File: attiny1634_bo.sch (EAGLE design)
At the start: 11 parts, among them J1 AVR_SPI_PRG_6NS, Y1 12MHz

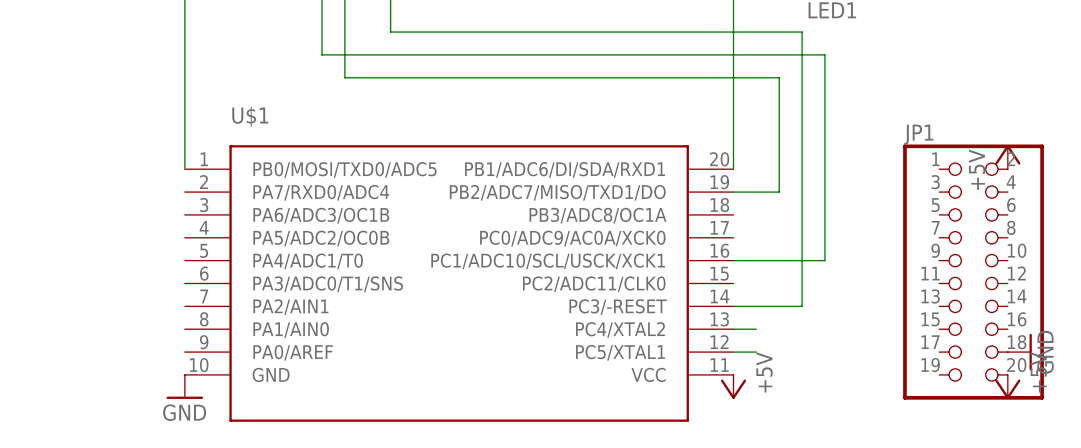
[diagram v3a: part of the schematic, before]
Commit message: connected portA
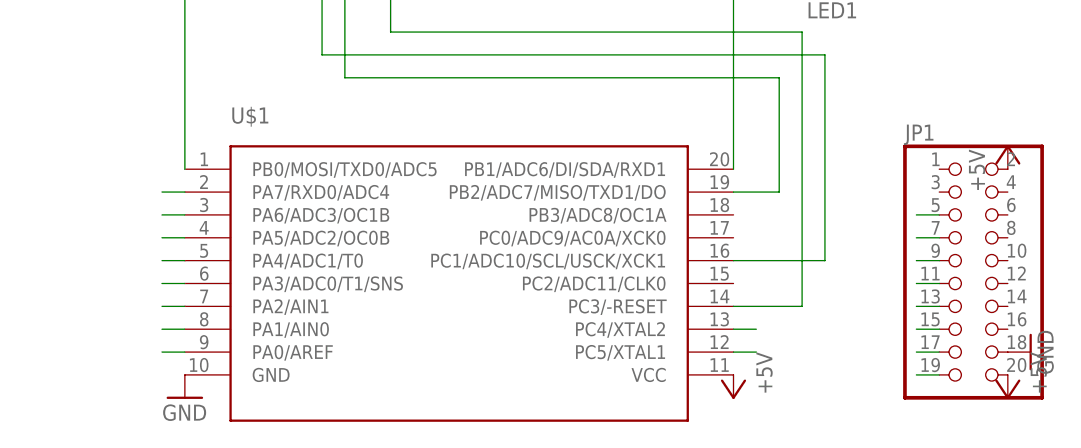
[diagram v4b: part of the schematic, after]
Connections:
- new net PA0: JP1.5, U$1.PA0/AREF
- new net PA1: JP1.7, U$1.PA1/AIN0
- new net PA2: JP1.9, U$1.PA2/AIN1
- new net PA3: JP1.11, U$1.PA3/ADC0/T1/SNS
- new net PA4: JP1.13, U$1.PA4/ADC1/T0
- new net PA5: JP1.15, U$1.PA5/ADC2/OC0B
- new net PA6: JP1.17, U$1.PA6/ADC3/OC1B
- new net PA7: JP1.19, U$1.PA7/RXD0/ADC4
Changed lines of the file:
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@@
+</segment>
+</net>
+<net name="PA0" class="0">
+<segment>
+<pinref part="U$1" gate="G$1" pin="PA0/AREF"/>
+<wire x1="35.56" y1="50.8" x2="33.02" y2="50.8" width="0.1524" layer="91"/>
+</segment>
+<segment>
+<pinref part="JP1" gate="A" pin="5"/>
+<wire x1="119.38" y1="66.04" x2="116.84" y2="66.04" width="0.1524" layer="91"/>
+</segment>
+</net>
+<net name="PA1" class="0">
+<segment>
+<pinref part="U$1" gate="G$1" pin="PA1/AIN0"/>
+<wire x1="35.56" y1="53.34" x2="33.02" y2="53.34" width="0.1524" layer="91"/>
+</segment>
+<segment>
+<pinref part="JP1" gate="A" pin="7"/>
+<wire x1="119.38" y1="63.5" x2="116.84" y2="63.5" width="0.1524" layer="91"/>
+</segment>
+</net>
+<net name="PA5" class="0">
+<segment>
+<pinref part="JP1" gate="A" pin="15"/>
+<wire x1="119.38" y1="53.34" x2="116.84" y2="53.34" width="0.1524" layer="91"/>
+</segment>
+<segment>
+<pinref part="U$1" gate="G$1" pin="PA5/ADC2/OC0B"/>
+<wire x1="35.56" y1="63.5" x2="33.02" y2="63.5" width="0.1524" layer="91"/>
+</segment>
+</net>
+<net name="PA4" class="0">
+<segment>
+<pinref part="JP1" gate="A" pin="13"/>
+<wire x1="119.38" y1="55.88" x2="116.84" y2="55.88" width="0.1524" layer="91"/>
+</segment>
+<segment>
+<pinref part="U$1" gate="G$1" pin="PA4/ADC1/T0"/>
+<wire x1="35.56" y1="60.96" x2="33.02" y2="60.96" width="0.1524" layer="91"/>
+</segment>
+</net>
+<net name="PA3" class="0">
+<segment>
+<pinref part="JP1" gate="A" pin="11"/>
+<wire x1="119.38" y1="58.42" x2="116.84" y2="58.42" width="0.1524" layer="91"/>
+</segment>
+<segment>
+<pinref part="U$1" gate="G$1" pin="PA3/ADC0/T1/SNS"/>
+<wire x1="35.56" y1="58.42" x2="33.02" y2="58.42" width="0.1524" layer="91"/>
+</segment>
+</net>
+<net name="PA2" class="0">
+<segment>
+<pinref part="JP1" gate="A" pin="9"/>
+<wire x1="119.38" y1="60.96" x2="116.84" y2="60.96" width="0.1524" layer="91"/>
+</segment>
+<segment>
+<pinref part="U$1" gate="G$1" pin="PA2/AIN1"/>
+<wire x1="35.56" y1="55.88" x2="33.02" y2="55.88" width="0.1524" layer="91"/>
+</segment>
+</net>
+<net name="PA7" class="0">
+<segment>
+<pinref part="JP1" gate="A" pin="19"/>
+<wire x1="119.38" y1="48.26" x2="116.84" y2="48.26" width="0.1524" layer="91"/>
+</segment>
+<segment>
+<pinref part="U$1" gate="G$1" pin="PA7/RXD0/ADC4"/>
+<wire x1="35.56" y1="68.58" x2="33.02" y2="68.58" width="0.1524" layer="91"/>
+</segment>
+</net>
+<net name="PA6" class="0">
+<segment>
+<pinref part="JP1" gate="A" pin="17"/>
+<wire x1="119.38" y1="50.8" x2="116.84" y2="50.8" width="0.1524" layer="91"/>
+</segment>
+<segment>
+<pinref part="U$1" gate="G$1" pin="PA6/ADC3/OC1B"/>
+<wire x1="35.56" y1="66.04" x2="33.02" y2="66.04" width="0.1524" layer="91"/>
 </segment>
 </net>

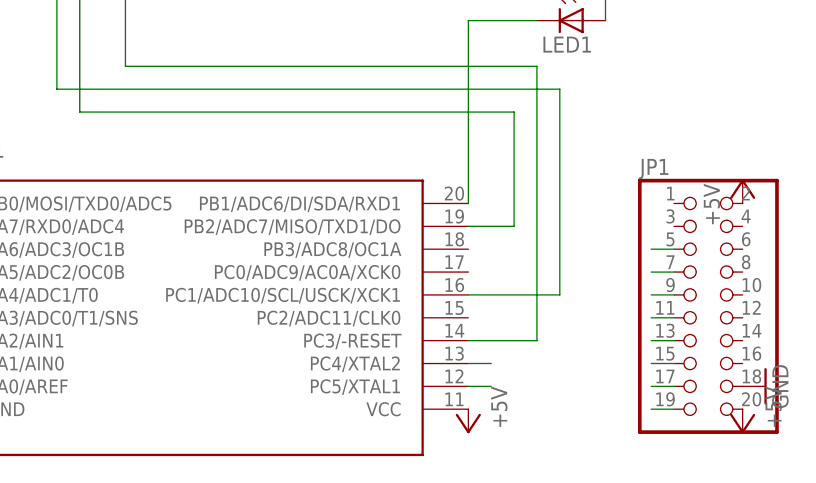
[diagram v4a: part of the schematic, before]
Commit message: typo fixes, connected portB
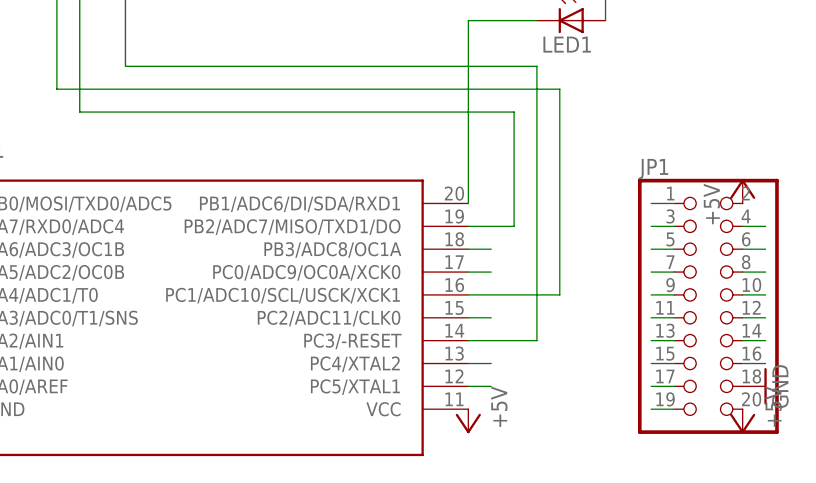
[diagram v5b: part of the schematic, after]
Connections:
- removed net PB1/ADC6: LED1.C, U$1.PB1/ADC6/DI/SDA/RXD1
- new net N$1: JP1.3
- new net N$2: U$1.PC2/ADC11/CLK0
- new net N$4: JP1.6
- new net N$5: JP1.4
- new net N$6: JP1.1
- new net PB1/ADC6/RX1: JP1.14, LED1.C, U$1.PB1/ADC6/DI/SDA/RXD1
- new net PB3/ADC8/OC1A: JP1.10, U$1.PB3/ADC8/OC1A
- new net PC0/ADC9/OC0A: JP1.8, U$1.PC0/ADC9/OC0A/XCK0
- net PB0/MOSI/TX0/ADC5: now also JP1.16
- net PB2/ADC7/TX1: now also JP1.12
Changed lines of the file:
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@@
 </segment>
 </net>
-<net name="PB1/ADC6" class="0">
+<net name="PB1/ADC6/RX1" class="0">
 <segment>
 <pinref part="LED1" gate="G$1" pin="C"/>
@@
 <pinref part="U$1" gate="G$1" pin="PB1/ADC6/DI/SDA/RXD1"/>
 <wire x1="96.52" y1="71.12" x2="96.52" y2="91.44" width="0.1524" layer="91"/>
+</segment>
+<segment>
+<pinref part="JP1" gate="A" pin="14"/>
+<wire x1="127" y1="55.88" x2="129.54" y2="55.88" width="0.1524" layer="91"/>
 </segment>
 </net>
@@
 <wire x1="83.82" y1="93.98" x2="35.56" y2="93.98" width="0.1524" layer="91"/>
 <wire x1="35.56" y1="93.98" x2="35.56" y2="71.12" width="0.1524" layer="91"/>
+</segment>
+<segment>
+<pinref part="JP1" gate="A" pin="16"/>
+<wire x1="127" y1="53.34" x2="129.54" y2="53.34" width="0.1524" layer="91"/>
 </segment>
 </net>
@@
 <wire x1="53.34" y1="109.22" x2="58.42" y2="109.22" width="0.1524" layer="91"/>
 </segment>
+<segment>
+<pinref part="JP1" gate="A" pin="12"/>
+<wire x1="127" y1="58.42" x2="129.54" y2="58.42" width="0.1524" layer="91"/>
+</segment>
 </net>
 <net name="PC3/-RESET" class="0">
@@
 </segment>
 </net>
+<net name="N$4" class="0">
+<segment>
+<pinref part="JP1" gate="A" pin="6"/>
+<wire x1="127" y1="66.04" x2="129.54" y2="66.04" width="0.1524" layer="91"/>
+</segment>
+</net>
+<net name="N$5" class="0">
+<segment>
+<pinref part="JP1" gate="A" pin="4"/>
+<wire x1="127" y1="68.58" x2="129.54" y2="68.58" width="0.1524" layer="91"/>
+</segment>
+</net>
+<net name="PB3/ADC8/OC1A" class="0">
+<segment>
+<pinref part="U$1" gate="G$1" pin="PB3/ADC8/OC1A"/>
+<wire x1="96.52" y1="66.04" x2="99.06" y2="66.04" width="0.1524" layer="91"/>
+</segment>
+<segment>
+<pinref part="JP1" gate="A" pin="10"/>
+<wire x1="127" y1="60.96" x2="129.54" y2="60.96" width="0.1524" layer="91"/>
+</segment>
+</net>
+<net name="PC0/ADC9/OC0A" class="0">
+<segment>
+<pinref part="U$1" gate="G$1" pin="PC0/ADC9/OC0A/XCK0"/>
+<wire x1="96.52" y1="63.5" x2="99.06" y2="63.5" width="0.1524" layer="91"/>
+</segment>
+<segment>
+<pinref part="JP1" gate="A" pin="8"/>
+<wire x1="127" y1="63.5" x2="129.54" y2="63.5" width="0.1524" layer="91"/>
+</segment>
+</net>
+<net name="N$2" class="0">
+<segment>
+<pinref part="U$1" gate="G$1" pin="PC2/ADC11/CLK0"/>
+<wire x1="96.52" y1="58.42" x2="99.06" y2="58.42" width="0.1524" layer="91"/>
+</segment>
+</net>
+<net name="N$1" class="0">
+<segment>
+<pinref part="JP1" gate="A" pin="3"/>
+<wire x1="119.38" y1="68.58" x2="116.84" y2="68.58" width="0.1524" layer="91"/>
+</segment>
+</net>
+<net name="N$6" class="0">
+<segment>
+<pinref part="JP1" gate="A" pin="1"/>
+<wire x1="119.38" y1="71.12" x2="116.84" y2="71.12" width="0.1524" layer="91"/>
+</segment>
+</net>

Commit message: more signals
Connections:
- removed net N$4: JP1.6
- removed net N$5: JP1.4
- net PC4/XTAL2: now also JP1.6
- net PC5/XTAL1: now also JP1.4
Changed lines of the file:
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@@
 <wire x1="15.24" y1="91.44" x2="25.4" y2="91.44" width="0.1524" layer="91"/>
+</segment>
+<segment>
+<pinref part="JP1" gate="A" pin="4"/>
+<wire x1="127" y1="68.58" x2="129.54" y2="68.58" width="0.1524" layer="91"/>
 </segment>
 </net>
@@
 <wire x1="25.4" y1="104.14" x2="25.4" y2="111.76" width="0.1524" layer="91"/>
 <wire x1="25.4" y1="111.76" x2="15.24" y2="111.76" width="0.1524" layer="91"/>
+</segment>
+<segment>
+<pinref part="JP1" gate="A" pin="6"/>
+<wire x1="127" y1="66.04" x2="129.54" y2="66.04" width="0.1524" layer="91"/>
 </segment>
 </net>
@@
 </segment>
 </net>
-<net name="N$4" class="0">
-<segment>
-<pinref part="JP1" gate="A" pin="6"/>
-<wire x1="127" y1="66.04" x2="129.54" y2="66.04" width="0.1524" layer="91"/>
-</segment>
-</net>
-<net name="N$5" class="0">
-<segment>
-<pinref part="JP1" gate="A" pin="4"/>
-<wire x1="127" y1="68.58" x2="129.54" y2="68.58" width="0.1524" layer="91"/>
-</segment>
-</net>

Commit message: adjusted texts and positions
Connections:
- removed net N$1: JP1.3
- removed net N$2: U$1.PC2/ADC11/CLK0
- removed net N$6: JP1.1
- new net PC2/ADC11: JP1.3, U$1.PC2/ADC11/CLK0
- net PC1/SCL/ADC10: now also JP1.1
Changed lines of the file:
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@@
 <wire x1="50.8" y1="106.68" x2="58.42" y2="106.68" width="0.1524" layer="91"/>
+</segment>
+<segment>
+<pinref part="JP1" gate="A" pin="1"/>
+<wire x1="119.38" y1="71.12" x2="116.84" y2="71.12" width="0.1524" layer="91"/>
 </segment>
 </net>
@@
 </segment>
 </net>
-<net name="N$2" class="0">
+<net name="PC2/ADC11" class="0">
 <segment>
 <pinref part="U$1" gate="G$1" pin="PC2/ADC11/CLK0"/>
 <wire x1="96.52" y1="58.42" x2="99.06" y2="58.42" width="0.1524" layer="91"/>
 </segment>
-</net>
-<net name="N$1" class="0">
 <segment>
 <pinref part="JP1" gate="A" pin="3"/>
@@
 </segment>
 </net>
-<net name="N$6" class="0">
-<segment>
-<pinref part="JP1" gate="A" pin="1"/>
-<wire x1="119.38" y1="71.12" x2="116.84" y2="71.12" width="0.1524" layer="91"/>
-</segment>
-</net>
